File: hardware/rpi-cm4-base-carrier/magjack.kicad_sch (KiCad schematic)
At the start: 7 parts, among them J5 THD-02-R, U3 TPD4EUSB30, U4 TPD4EUSB30, U5 MagJack-A70-112-331N126

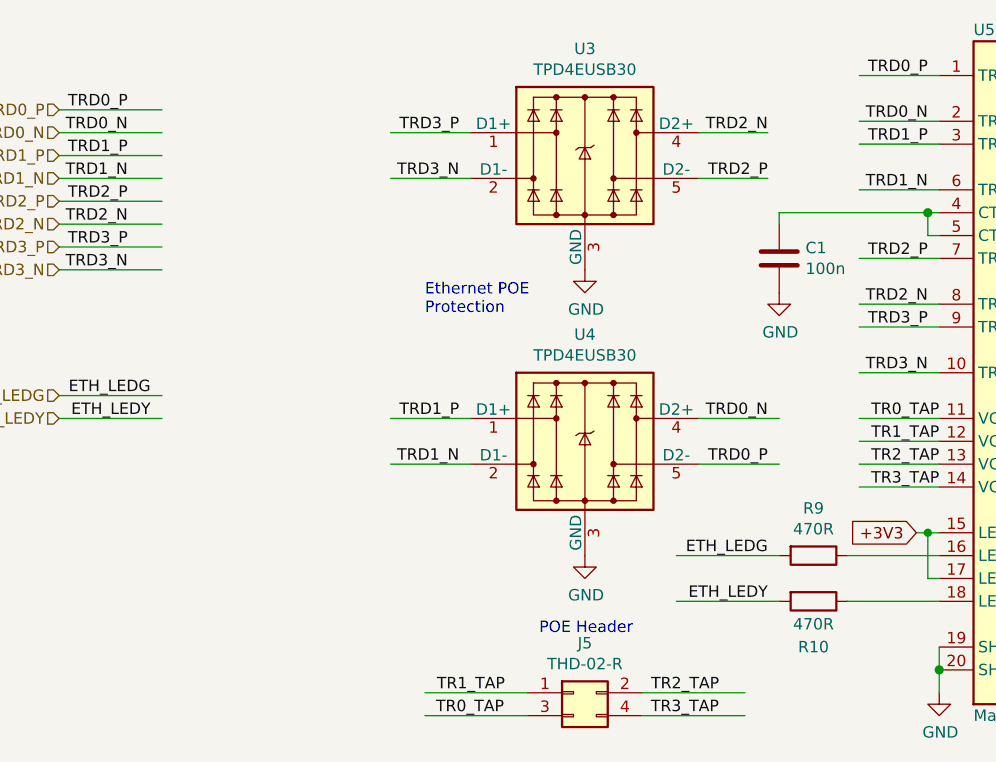
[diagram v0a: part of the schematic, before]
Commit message: routing for some modules progressing quickly, USBHUB mostly complete, thought needed regarding which connectors should be exposed post assembly and which should be for internal use only. LED identifiers and buttons still missing
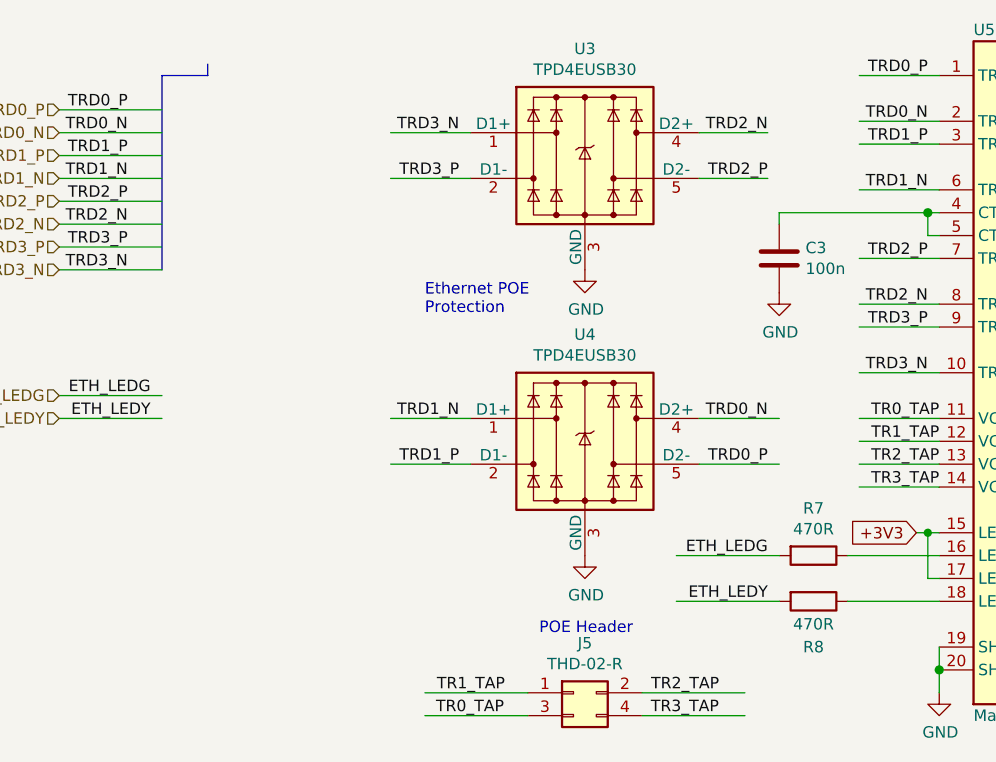
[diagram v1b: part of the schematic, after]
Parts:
- renumbered C1 to C3, R9 to R7, R10 to R8
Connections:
- net TRD1_N: now also U4.1 (D1+), U4.10; no longer U4.2 (D1-), U4.9
- net TRD1_P: now also U4.2 (D1-), U4.9; no longer U4.1 (D1+), U4.10
- net TRD3_N: now also U3.1 (D1+), U3.10; no longer U3.2 (D1-), U3.9
- net TRD3_P: now also U3.2 (D1-), U3.9; no longer U3.1 (D1+), U3.10
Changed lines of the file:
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@@
     (stroke (width 0) (type solid))
+  )
+  (bus (pts (xy 82.55 59.69) (xy 77.47 59.69))
+    (stroke (width 0) (type default))
   )
   (wire (pts (xy 154.94 87.63) (xy 163.83 87.63))
@@
   (wire (pts (xy 146.05 74.93) (xy 162.56 74.93))
     (stroke (width 0) (type solid))
+  )
+  (bus (pts (xy 82.55 59.69) (xy 82.55 58.42))
+    (stroke (width 0) (type default))
   )
   (wire (pts (xy 102.87 66.04) (xy 111.76 66.04))
@@
     (stroke (width 0) (type solid))
   )
+  (bus (pts (xy 77.47 59.69) (xy 77.47 81.28))
+    (stroke (width 0) (type default))
+  )
   (wire (pts (xy 153.67 118.11) (xy 163.83 118.11))
     (stroke (width 0) (type solid))
@@
     (effects (font (size 1.27 1.27)) (justify right bottom))
   )
-  (label "TRD1_P" (at 110.49 97.79 180) (fields_autoplaced)
+  (label "TRD1_N" (at 110.49 97.79 180) (fields_autoplaced)
     (effects (font (size 1.27 1.27)) (justify right bottom))
   )
@@
     (effects (font (size 1.27 1.27)) (justify right bottom))
   )
-  (label "TRD3_N" (at 110.49 71.12 180) (fields_autoplaced)
+  (label "TRD3_P" (at 110.49 71.12 180) (fields_autoplaced)
     (effects (font (size 1.27 1.27)) (justify right bottom))
   )
@@
     (effects (font (size 1.27 1.27)) (justify right bottom))
   )
-  (label "TRD1_N" (at 110.49 102.87 180) (fields_autoplaced)
-    (effects (font (size 1.27 1.27)) (justify right bottom))
-  )
-  (label "TRD3_P" (at 110.49 66.04 180) (fields_autoplaced)
+  (label "TRD1_P" (at 110.49 102.87 180) (fields_autoplaced)
+    (effects (font (size 1.27 1.27)) (justify right bottom))
+  )
+  (label "TRD3_N" (at 110.49 66.04 180) (fields_autoplaced)
     (effects (font (size 1.27 1.27)) (justify right bottom))
   )
@@
     (effects (font (size 1.27 1.27)) (justify right))
   )
+  (netclass_flag "" (length 2.54) (shape round) (at 82.55 58.42 0) (fields_autoplaced)
+    (effects (font (size 1.27 1.27)) (justify left bottom))
+    (property "Netclass" "ETH 100R Diff" (at 83.439 55.88 0)
+      (effects (font (size 1.27 1.27) italic) (justify left))
+    )
+  )
   (symbol (lib_id "power:GND") (at 124.46 113.03 0) (unit 1)
     (in_bom yes) (on_board yes) (dnp no)
-    (property "Reference" "#PWR02" (at 124.46 119.38 0)
+    (property "Reference" "#PWR018" (at 124.46 119.38 0)
       (effects (font (size 1.27 1.27)) hide)
     )
@@
       (project "rpi-cm4-base-carrier"
         (path "/92c58705-ecb0-498b-b561-44a3f0daad57/f59b312f-519e-4202-b8b6-d9dde16427a9"
-          (reference "#PWR02") (unit 1)
+          (reference "#PWR018") (unit 1)
         )
       )
@@
   (symbol (lib_id "Device:C") (at 146.05 80.01 0) (unit 1)
     (in_bom yes) (on_board yes) (dnp no)
-    (property "Reference" "C1" (at 148.971 78.8416 0)
+    (property "Reference" "C3" (at 148.971 78.8416 0)
       (effects (font (size 1.27 1.27)) (justify left))
     )
@@
       (project "rpi-cm4-base-carrier"
         (path "/92c58705-ecb0-498b-b561-44a3f0daad57/f59b312f-519e-4202-b8b6-d9dde16427a9"
+          (reference "C3") (unit 1)
+        )
+      )
+      (project "CM4IOv5"
+        (path "/e63e39d7-6ac0-4ffd-8aa3-1841a4541b55/00000000-0000-0000-0000-00005cff706a"
           (reference "C1") (unit 1)
         )
       )
-      (project "CM4IOv5"
-        (path "/e63e39d7-6ac0-4ffd-8aa3-1841a4541b55/00000000-0000-0000-0000-00005cff706a"
-          (reference "C1") (unit 1)
-        )
-      )
     )
   )
   (symbol (lib_id "power:GND") (at 124.46 81.28 0) (unit 1)
     (in_bom yes) (on_board yes) (dnp no)
-    (property "Reference" "#PWR01" (at 124.46 87.63 0)
+    (property "Reference" "#PWR017" (at 124.46 87.63 0)
       (effects (font (size 1.27 1.27)) hide)
     )
@@
       (project "rpi-cm4-base-carrier"
         (path "/92c58705-ecb0-498b-b561-44a3f0daad57/f59b312f-519e-4202-b8b6-d9dde16427a9"
-          (reference "#PWR01") (unit 1)
+          (reference "#PWR017") (unit 1)
         )
       )
@@
   (symbol (lib_id "Device:R") (at 149.86 113.03 270) (unit 1)
     (in_bom yes) (on_board yes) (dnp no)
-    (property "Reference" "R9" (at 149.86 107.7722 90)
+    (property "Reference" "R7" (at 149.86 107.7722 90)
       (effects (font (size 1.27 1.27)))
     )
@@
       (project "rpi-cm4-base-carrier"
         (path "/92c58705-ecb0-498b-b561-44a3f0daad57/f59b312f-519e-4202-b8b6-d9dde16427a9"
-          (reference "R9") (unit 1)
+          (reference "R7") (unit 1)
         )
       )
@@
   (symbol (lib_id "power:GND") (at 146.05 83.82 0) (unit 1)
     (in_bom yes) (on_board yes) (dnp no)
-    (property "Reference" "#PWR03" (at 146.05 90.17 0)
+    (property "Reference" "#PWR019" (at 146.05 90.17 0)
       (effects (font (size 1.27 1.27)) hide)
     )
@@
       (project "rpi-cm4-base-carrier"
         (path "/92c58705-ecb0-498b-b561-44a3f0daad57/f59b312f-519e-4202-b8b6-d9dde16427a9"
-          (reference "#PWR03") (unit 1)
+          (reference "#PWR019") (unit 1)
         )
       )
@@
   (symbol (lib_id "power:GND") (at 163.83 128.27 0) (unit 1)
     (in_bom yes) (on_board yes) (dnp no)
-    (property "Reference" "#PWR04" (at 163.83 134.62 0)
+    (property "Reference" "#PWR020" (at 163.83 134.62 0)
       (effects (font (size 1.27 1.27)) hide)
     )
@@
       (project "rpi-cm4-base-carrier"
         (path "/92c58705-ecb0-498b-b561-44a3f0daad57/f59b312f-519e-4202-b8b6-d9dde16427a9"
-          (reference "#PWR04") (unit 1)
+          (reference "#PWR020") (unit 1)
         )
       )
@@
   (symbol (lib_id "Device:R") (at 149.86 118.11 270) (unit 1)
     (in_bom yes) (on_board yes) (dnp no)
-    (property "Reference" "R10" (at 149.86 123.19 90)
+    (property "Reference" "R8" (at 149.86 123.19 90)
       (effects (font (size 1.27 1.27)))
     )
@@
       (project "rpi-cm4-base-carrier"
         (path "/92c58705-ecb0-498b-b561-44a3f0daad57/f59b312f-519e-4202-b8b6-d9dde16427a9"
-          (reference "R10") (unit 1)
-        )
-      )
+          (reference "R8") (unit 1)
+        )
+      )

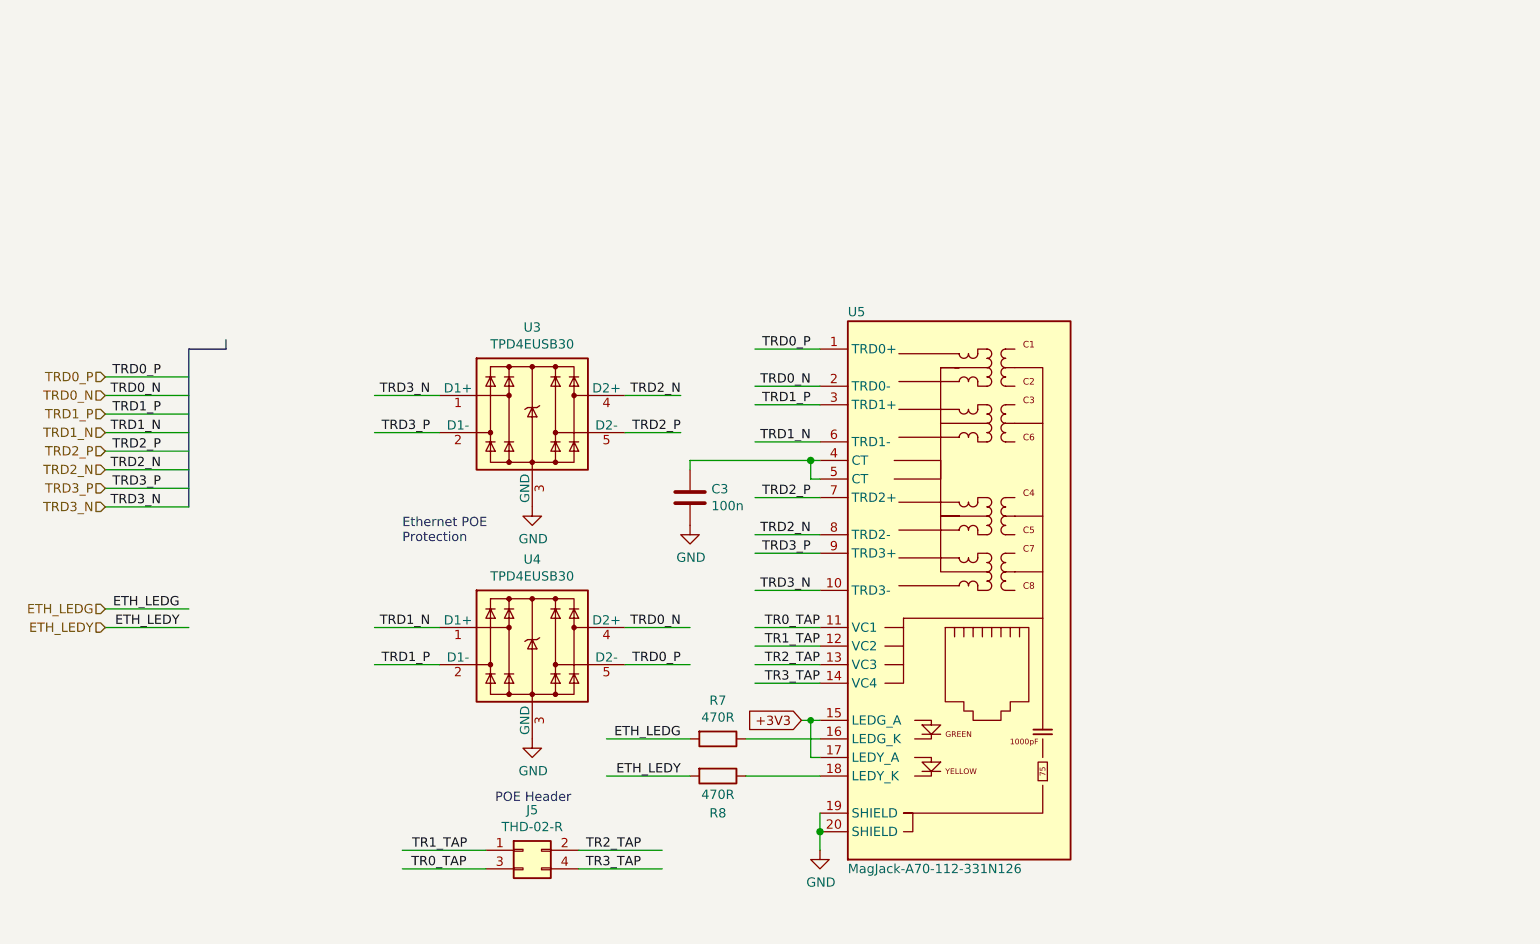
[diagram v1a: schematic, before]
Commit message: started final placement of blocks, realised ESD suppression devices cannot be manufactured with JLC, need to switch part
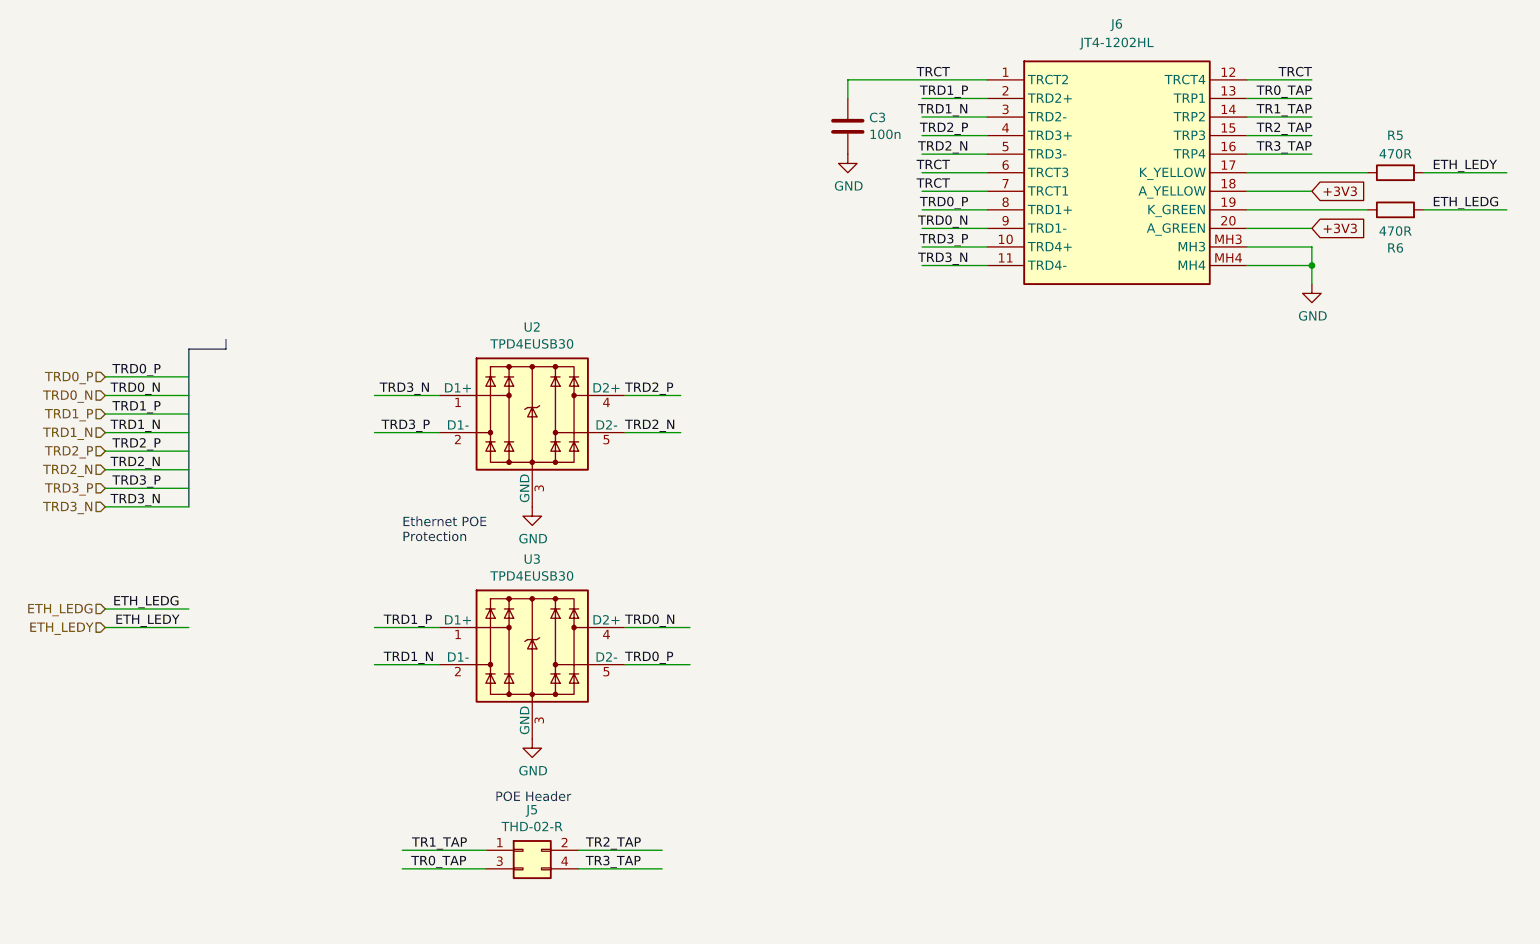
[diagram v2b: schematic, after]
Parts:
- removed R7, R8: 470R, Resistor_SMD:R_0402_1005Metric, symbol Device:R
- removed U5: MagJack-A70-112-331N126, CM4IO:TRJG0926HENL, symbol CM4IO:MagJack-A70-112-331N126
- added J6: JT4-1202HL, JT41202HL, symbol SamacSys_Parts:JT4-1202HL
- added R5, R6: 470R, Resistor_SMD:R_0402_1005Metric, symbol Device:R
- renumbered U3 to U2, U4 to U3
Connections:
- net +3V3: now also J6.18 (A_YELLOW), J6.20 (A_GREEN)
- net ETH_LEDG: now also R6.2
- net ETH_LEDY: now also R5.2
- net GND: now also J6.MH3, J6.MH4
- net TR0_TAP: now also J6.13 (TRP1)
- net TR1_TAP: now also J6.14 (TRP2)
- net TR2_TAP: now also J6.15 (TRP3)
- net TR3_TAP: now also J6.16 (TRP4)
- net TRD0_N: now also J6.9 (TRD1-)
- net TRD0_P: now also J6.8 (TRD1+)
- net TRD1_N: now also U3.2 (D1-), U3.9, J6.3 (TRD2-); no longer U3.1 (D1+), U3.10
- net TRD1_P: now also U3.1 (D1+), U3.10, J6.2 (TRD2+); no longer U3.2 (D1-), U3.9
- net TRD2_N: now also U2.5 (D2-), U2.6, J6.5 (TRD3-); no longer U2.4 (D2+), U2.7
- net TRD2_P: now also U2.4 (D2+), U2.7, J6.4 (TRD3+); no longer U2.5 (D2-), U2.6
- net TRD3_N: now also J6.11 (TRD4-)
- net TRD3_P: now also J6.10 (TRD4+)
- net TRCT: now reaches C3.1
- net TRCT: now also J6.1 (TRCT2), J6.12 (TRCT4), J6.6 (TRCT3), J6.7 (TRCT1)
- new net: J6.17 (K_YELLOW), R5.1
- new net: J6.19 (K_GREEN), R6.1

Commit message: started to route core connectors to CM4, RJ45 annoyingly has the inverse pinout to CM4, need to work out how to uncross tracking sensibly
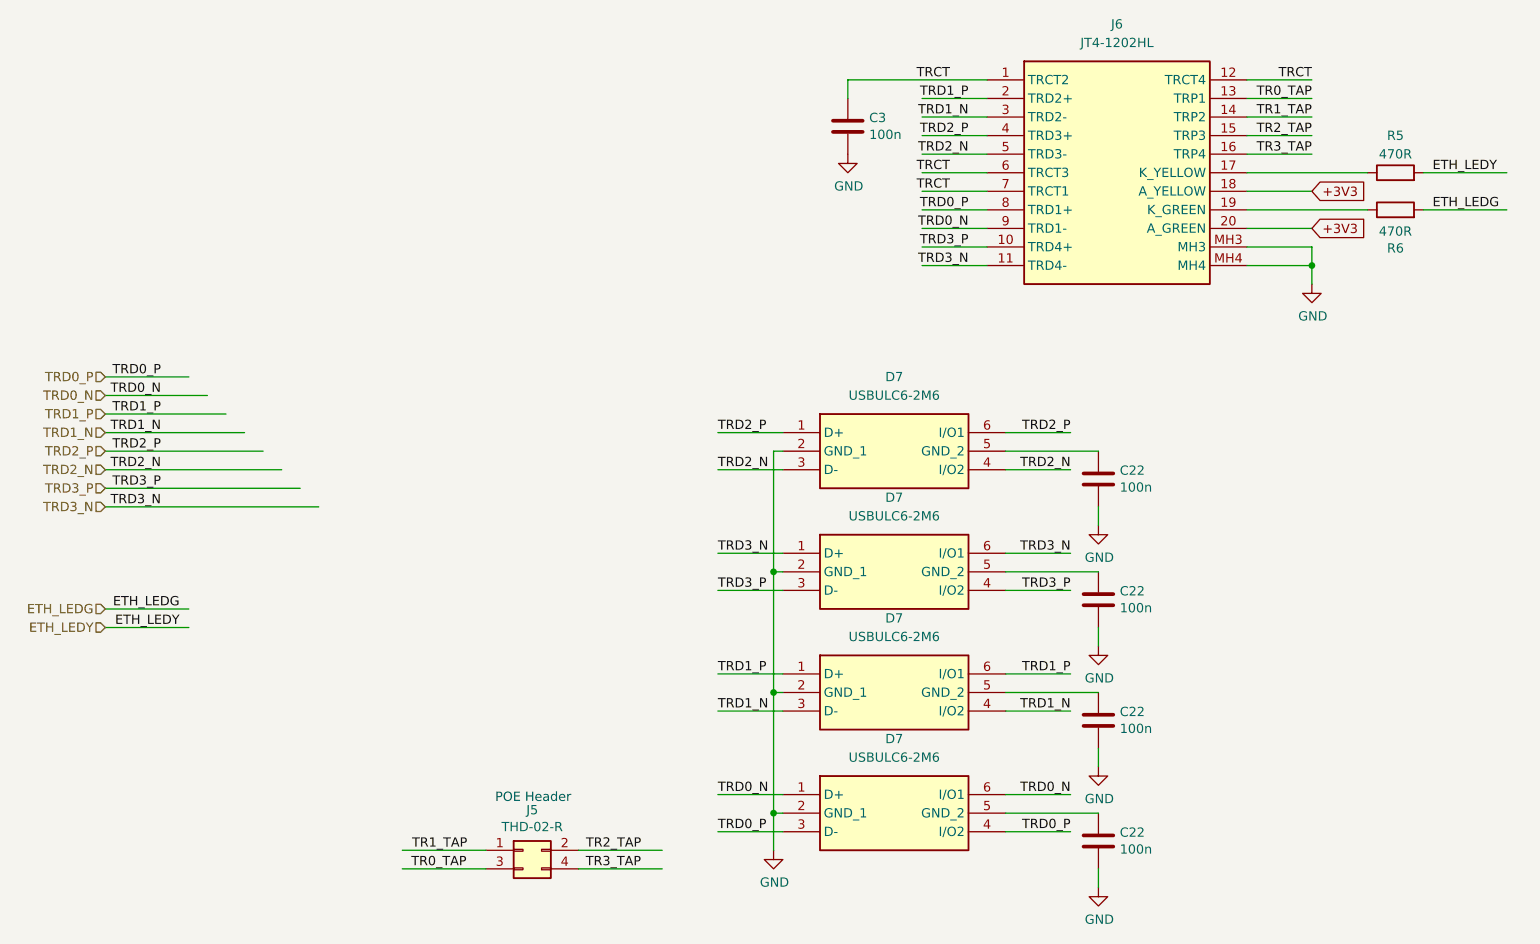
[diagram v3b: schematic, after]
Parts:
- removed U2, U3: TPD4EUSB30, Package_SON:USON-10_2.5x1.0mm_P0.5mm, symbol CM4IO:TPD4EUSB30
- added C22 (x4): 100n, Capacitor_SMD:C_0402_1005Metric, symbol Device:C
- added D7 (x4): USBULC6-2M6, SON50P100X145X60-6N-D, symbol SamacSys_Parts:USBULC6-2M6
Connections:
- net GND: now also C22.2, C22.2, C22.2, C22.2, D7.2 (GND_1), D7.2 (GND_1), D7.2 (GND_1), D7.2 (GND_1)
- net TRD0_N: now also D7.1 (D+), D7.6 (I/O1)
- net TRD0_P: now also D7.3 (D-), D7.4 (I/O2)
- net TRD1_N: now also D7.3 (D-), D7.4 (I/O2)
- net TRD1_P: now also D7.1 (D+), D7.6 (I/O1)
- net TRD2_N: now also D7.3 (D-), D7.4 (I/O2)
- net TRD2_P: now also D7.1 (D+), D7.6 (I/O1)
- net TRD3_N: now also D7.1 (D+), D7.6 (I/O1)
- net TRD3_P: now also D7.3 (D-), D7.4 (I/O2)
- new net: C22.1, D7.5 (GND_2) (x4)
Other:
- note removed: "Ethernet POE Protection"

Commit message: schematic entry for samtec board edge connector complete, started breakout of GPIO lines for connection to board edge connector
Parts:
- D7: footprint SON50P100X145X60-6N-D -> SamacSys_Parts:SON50P100X145X60-6N-D
- J6: footprint JT41202HL -> SamacSys_Parts:JT41202HL
